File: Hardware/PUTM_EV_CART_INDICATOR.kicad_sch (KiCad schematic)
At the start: 17 parts, among them J1 Screw_Terminal_01x08, K3 IM07DTS, K4 IM07DTS

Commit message: Poprawiono schemat
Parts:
- removed D1: D, Diode_SMD:D_0603_1608Metric_Pad1.05x0.95mm_HandSolder, symbol Device:D
- removed R11, R12: 1K, Resistor_SMD:R_0603_1608Metric_Pad0.98x0.95mm_HandSolder, symbol Device:R_Small
- added D5, D6: D, Diode_SMD:D_MicroSMP_AK, symbol Device:D
- added F1: Fuse_Small, Fuse:Fuse_2920_7451Metric_Pad2.10x5.45mm_HandSolder, symbol Device:Fuse_Small
- added JP1: Jumper_2_Open, Jumper:SolderJumper-2_P1.3mm_Open_RoundedPad1.0x1.5mm, symbol Jumper:Jumper_2_Open
- added Q1: PMOS, symbol Simulation_SPICE:PMOS
- added R1: R_Small, symbol Device:R_Small
- D2: footprint Diode_SMD:D_0603_1608Metric_Pad1.05x0.95mm_HandSolder -> Diode_SMD:D_MicroSMP_AK
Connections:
- net +24V: now also JP1.1 (A), Q1.1 (D); no longer D2.1 (K), K3.1 (COIL_1), K3.3 (COM_1), K3.6 (COM_2), K4.1 (COIL_1), K4.3 (COM_1), K4.6 (COM_2)
- net GND: now also R1.2
- net IMD_LED: no longer D4.2 (A)
- net TSAL_LED: no longer D3.2 (A)
- net at K4.8 (COIL_2), Q4.3 (D): now also D6.2 (A)
- net current_driver/Input: now reaches K4.7 (NC_2)
- net current_driver2/Input: now reaches K3.4 (NO_1)
- new net: D5.2 (A), Q1.2 (G), R1.1
- new net: D5.1 (K), F1.2, Q1.3 (S)
- new net 24V_fused: D2.1 (K), D6.1 (K), F1.1, JP1.2 (B), K3.1 (COIL_1), K3.3 (COM_1), K3.6 (COM_2), K4.1 (COIL_1), K4.3 (COM_1), K4.6 (COM_2)
- new net current_driver/Output: D4.2 (A)
- new net current_driver2/Output: D3.2 (A)
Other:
- added sheet current_driver (current_driver.kicad_sch)
- added sheet current_driver1 (current_driver.kicad_sch)
- added sheet current_driver2 (current_driver.kicad_sch)
- added sheet current_driver3 (current_driver.kicad_sch)
- moved on the sheet: D3, D4, J1, Q4, Q5, R10, R22, R6, R8

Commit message: Wersja 2.0 do sprawdzenia :3
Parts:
- added C1, C2: NC, Capacitor_SMD:C_0603_1608Metric_Pad1.08x0.95mm_HandSolder, symbol Device:C_Small
- added H3, H4: MountingHole, MountingHole:MountingHole_2.2mm_M2, symbol Mechanical:MountingHole
- D2, D5, D6: footprint Diode_SMD:D_MicroSMP_AK -> Diode_SMD:Nexperia_CFP3_SOD-123W
- F1: value Fuse_Small -> 1.5A PPTC fuse; footprint Fuse:Fuse_2920_7451Metric_Pad2.10x5.45mm_HandSolder -> Library:Fuse_2920_7451Metric_Pad2.10x5.45mm_HandSolder
- Q1: footprint (none) -> Package_TO_SOT_SMD:SOT-223
- R1: footprint (none) -> Resistor_SMD:R_0603_1608Metric_Pad0.98x0.95mm_HandSolder
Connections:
- net +24V: now also Q1.2 (D); no longer Q1.1 (D)
- net GND: now also C1.2, C2.2
- net at D5.2 (A), R1.1: now also Q1.1 (G); no longer Q1.2 (G)
- net at Q4.1 (G), R10.1, R22.1: now also C2.1
- net at Q5.1 (G), R6.1, R8.2: now also C1.1
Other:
- moved on the sheet: D4, K4, Q4, R10, R22, R6

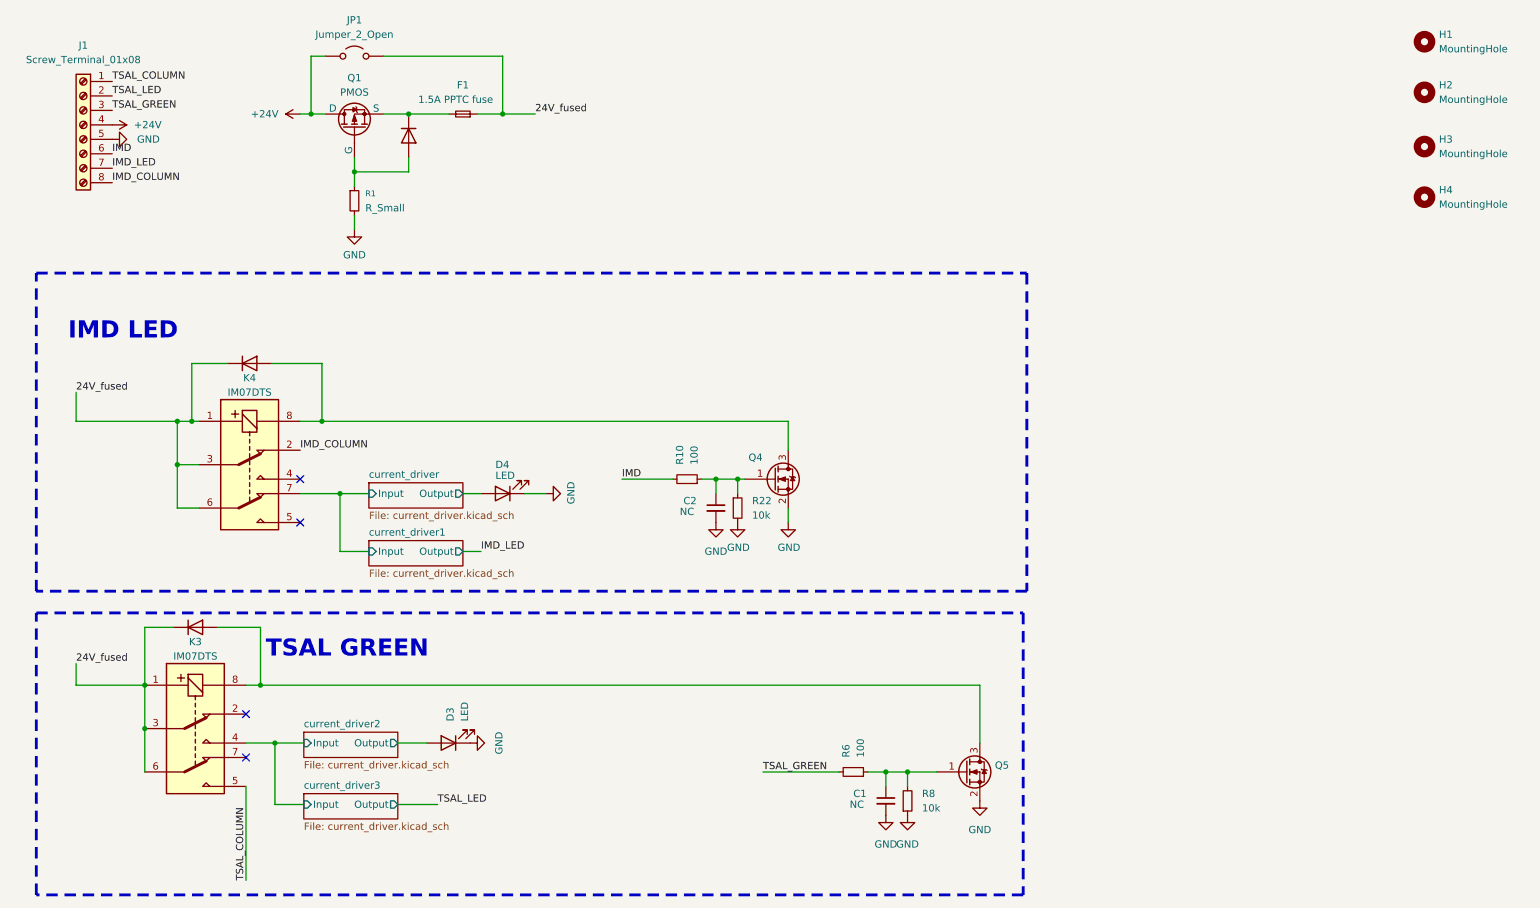
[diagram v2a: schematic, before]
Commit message: Dodano esd protection, zmieniono komponenty, poprawiono schemat itp
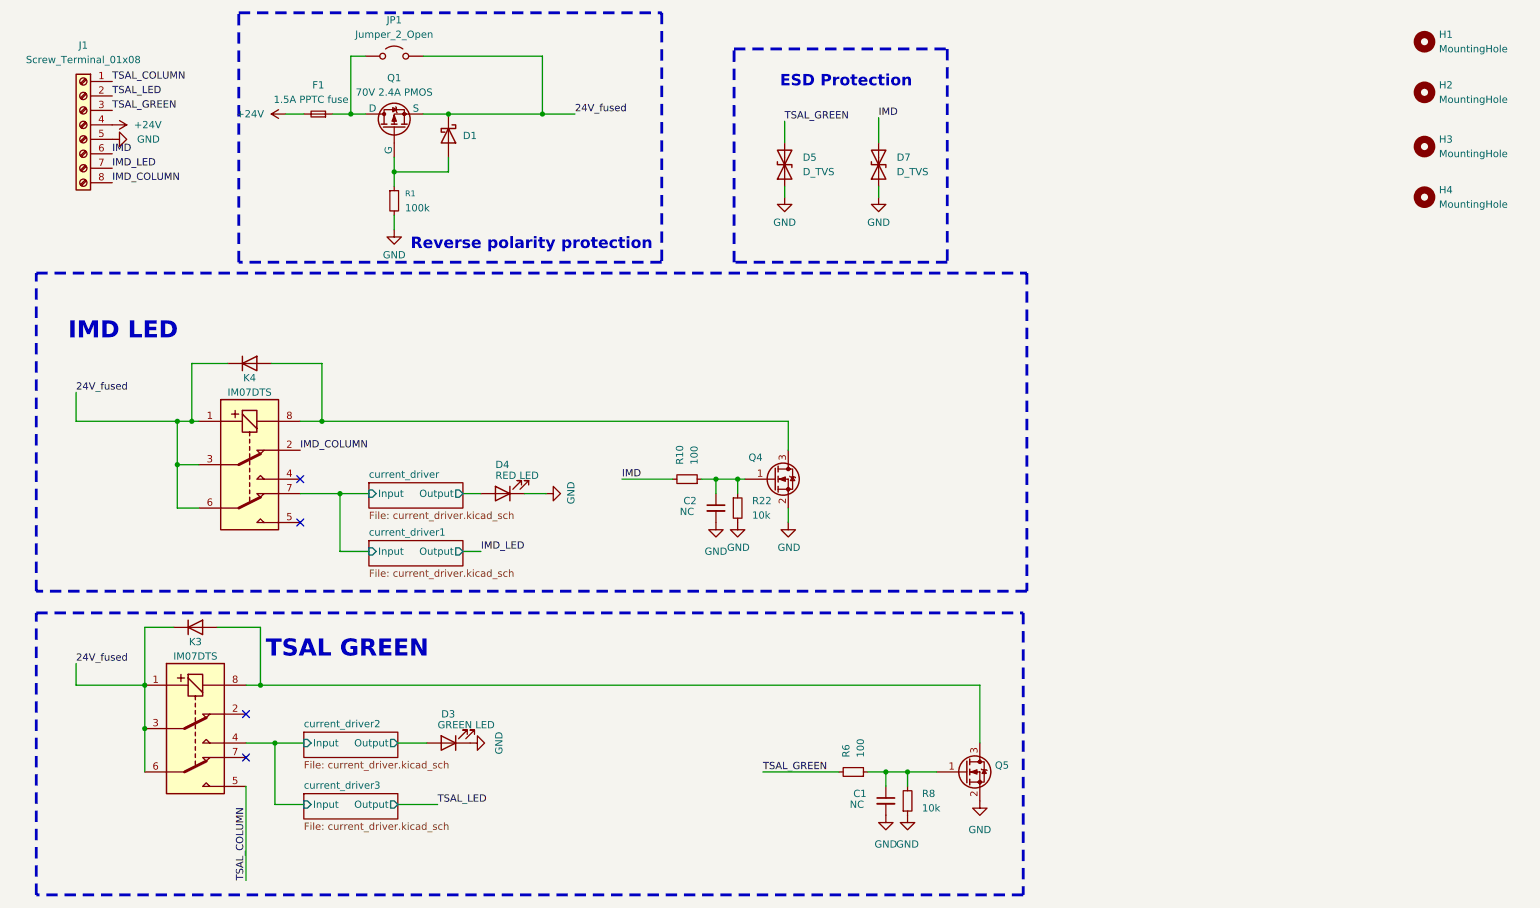
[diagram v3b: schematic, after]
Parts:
- removed D5: D, Diode_SMD:Nexperia_CFP3_SOD-123W, symbol Device:D
- added D1: D_Schottky, Diode_SMD:Nexperia_CFP3_SOD-123W, symbol Device:D_Schottky
- added D5, D7: D_TVS, Diode_SMD:D_SMA, symbol Device:D_TVS
- D3: value LED -> GREEN LED
- D4: value LED -> RED LED
- Q1: value PMOS -> 70V 2.4A PMOS
- R1: value R_Small -> 100k
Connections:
- net +24V: now also F1.2; no longer JP1.1 (A), Q1.2 (D)
- net 24V_fused: now also Q1.3 (S), D1.1 (K); no longer F1.1
- net GND: now also D5.1 (A1), D7.1 (A1)
- net IMD: now also D7.2 (A2)
- net TSAL_GREEN: now also D5.2 (A2)
- net at Q1.1 (G), R1.1: now also D1.2 (A)
- new net: F1.1, JP1.1 (A), Q1.2 (D)
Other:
- note added: "ESD Protection"
- note added: "Reverse polarity protection"
- moved on the sheet: F1, JP1, Q1, R1

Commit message: Dodano TVS na kazde wejscie, zmieniono diode w reverse polarity protection na zenera
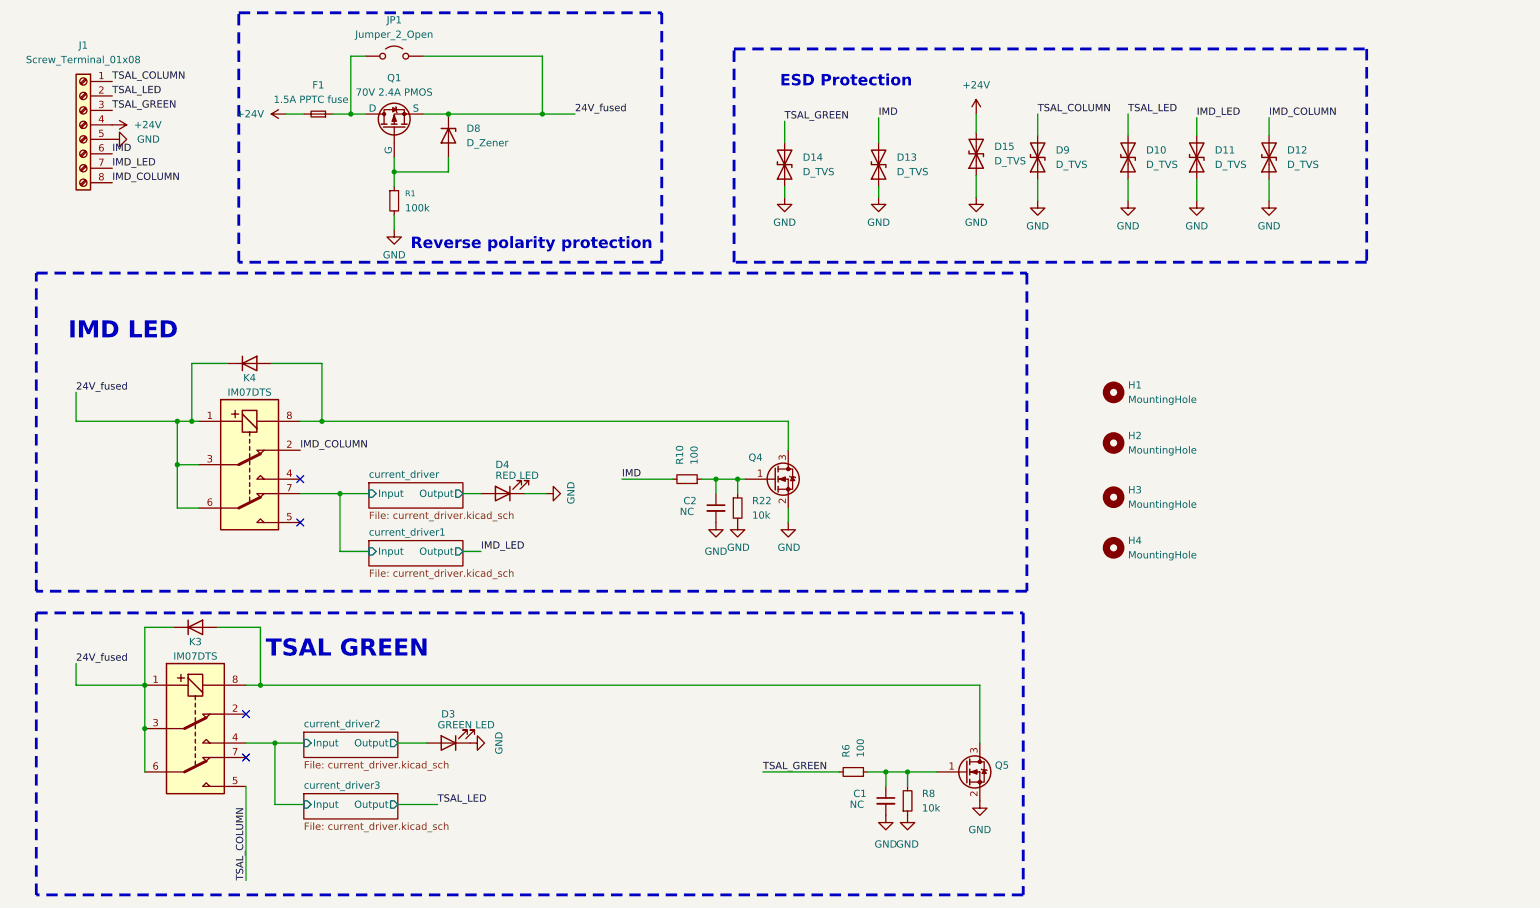
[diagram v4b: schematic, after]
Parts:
- removed D1: D_Schottky, Diode_SMD:Nexperia_CFP3_SOD-123W, symbol Device:D_Schottky
- removed D5, D7: D_TVS, Diode_SMD:D_SMA, symbol Device:D_TVS
- added D10, D11, D12, D13, D14, D15, D9: D_TVS, Include:SM4T82AY, symbol Device:D_TVS
- added D8: D_Zener, Include:SODFL5026X125N, symbol Device:D_Zener
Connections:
- net +24V: now also D15.2 (A2)
- net 24V_fused: now also D8.1 (K)
- net GND: now also D10.1 (A1), D11.1 (A1), D12.1 (A1), D13.1 (A1), D14.1 (A1), D15.1 (A1), D9.1 (A1)
- net IMD: now also D13.2 (A2)
- net IMD_COLUMN: now also D12.2 (A2)
- net IMD_LED: now also D11.2 (A2)
- net TSAL_COLUMN: now also D9.2 (A2)
- net TSAL_GREEN: now also D14.2 (A2)
- net TSAL_LED: now also D10.2 (A2)
- net at Q1.1 (G), R1.1: now also D8.2 (A)
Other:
- moved on the sheet: H1, H2, H3, H4
